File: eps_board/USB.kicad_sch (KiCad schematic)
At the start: 3 parts, among them J12 10155435-00011LF

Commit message: combine interrupts per powerline and use i2c expanders to turn on and solicit feedback
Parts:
- renumbered R122 to R98, R123 to R99
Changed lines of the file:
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@@
 		(dnp no)
 		(fields_autoplaced yes)
-		(property "Reference" "#PWR029"
+		(property "Reference" "#PWR033"
 			(at 114.3 89.535 0)
 			(effects
@@
 			(project "EPS"
 				(path "/05170af6-30ef-4c3a-b972-f098085da1bc/dffa178b-07a8-4735-b10c-32a6042c7f6e"
-					(reference "#PWR029")
+					(reference "#PWR033")
 					(unit 1)
 				)
@@
 		(on_board yes)
 		(dnp no)
-		(property "Reference" "R123"
+		(property "Reference" "R99"
 			(at 166.37 95.885 90)
 			(effects
@@
 			(project "EPS"
 				(path "/05170af6-30ef-4c3a-b972-f098085da1bc/dffa178b-07a8-4735-b10c-32a6042c7f6e"
-					(reference "R123")
+					(reference "R99")
 					(unit 1)
 				)
@@
 		(on_board yes)
 		(dnp no)
-		(property "Reference" "R122"
+		(property "Reference" "R98"
 			(at 120.65 80.645 90)
 			(effects
@@
 			(project "EPS"
 				(path "/05170af6-30ef-4c3a-b972-f098085da1bc/dffa178b-07a8-4735-b10c-32a6042c7f6e"
-					(reference "R122")
+					(reference "R98")
 					(unit 1)
 				)
@@
 		(dnp no)
 		(fields_autoplaced yes)
-		(property "Reference" "#PWR030"
+		(property "Reference" "#PWR034"
 			(at 172.72 99.695 0)
 			(effects
@@
 			(project "EPS"
 				(path "/05170af6-30ef-4c3a-b972-f098085da1bc/dffa178b-07a8-4735-b10c-32a6042c7f6e"
-					(reference "#PWR030")
+					(reference "#PWR034")
 					(unit 1)
 				)
@@
 		(dnp no)
 		(fields_autoplaced yes)
-		(property "Reference" "#PWR031"
+		(property "Reference" "#PWR035"
 			(at 161.29 117.475 0)
 			(effects
@@
 			(project "EPS"
 				(path "/05170af6-30ef-4c3a-b972-f098085da1bc/dffa178b-07a8-4735-b10c-32a6042c7f6e"
-					(reference "#PWR031")
+					(reference "#PWR035")
 					(unit 1)
 				)

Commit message: laying all the tracks, interim commit
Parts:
- added D1: ESD9B5.0ST5G, Diode_SMD:D_SOD-923, symbol Diode:ESD9B5.0ST5G
- added R167: 1M, Resistor_SMD:R_0402_1005Metric_Pad0.72x0.64mm_HandSolder, symbol Device:R
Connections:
- net GND: now also D1.2 (A2), R167.2
- net VBUS: now also D1.1 (A1), R167.1

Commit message: interim commit
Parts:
- added R1: 47K, Resistor_SMD:R_0402_1005Metric_Pad0.72x0.64mm_HandSolder, symbol Device:R
- R167: value 1M -> 91K
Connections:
- net VBUS: now also R1.1; no longer R167.1
- new net VBUS_GOOD: R1.2, R167.1
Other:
- moved on the sheet: R167
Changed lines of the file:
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@@
 	(paper "A4")
-	(junction
-		(at 189.865 83.185)
-		(diameter 0)
-		(color 0 0 0 0)
-	)
 	(junction
 		(at 177.165 78.105)
@@
 		(color 0 0 0 0)
 	)
-	(junction
-		(at 186.69 78.105)
-		(diameter 0)
-		(color 0 0 0 0)
-	)
 	(no_connect
 		(at 161.29 106.045)
@@
 	(wire
 		(pts
-			(xy 189.865 83.82) (xy 189.865 83.185)
-		)
-		(stroke
-			(width 0)
-			(type default)
-		)
-	)
-	(wire
-		(pts
-			(xy 189.865 83.185) (xy 191.135 83.185)
-		)
-		(stroke
-			(width 0)
-			(type default)
-		)
-	)
-	(wire
-		(pts
-			(xy 177.165 78.105) (xy 186.69 78.105)
+			(xy 177.165 78.105) (xy 191.135 78.105)
 		)
 		(stroke
@@
 	(wire
 		(pts
-			(xy 189.865 92.075) (xy 189.865 91.44)
-		)
-		(stroke
-			(width 0)
-			(type default)
-		)
-	)
-	(wire
-		(pts
-			(xy 186.69 83.185) (xy 189.865 83.185)
+			(xy 191.135 100.965) (xy 191.135 99.695)
 		)
 		(stroke
@@
 	(wire
 		(pts
+			(xy 191.135 88.265) (xy 191.135 92.075)
+		)
+		(stroke
+			(width 0)
+			(type default)
+		)
+	)
+	(wire
+		(pts
 			(xy 177.165 86.36) (xy 177.165 85.725)
 		)
@@
 	(wire
 		(pts
-			(xy 186.69 78.105) (xy 186.69 83.185)
-		)
-		(stroke
-			(width 0)
-			(type default)
-		)
-	)
-	(wire
-		(pts
-			(xy 186.69 78.105) (xy 191.135 78.105)
+			(xy 191.135 78.105) (xy 191.135 80.645)
 		)
 		(stroke
@@
 		)
 	)
+	(hierarchical_label "VBUS_GOOD"
+		(shape input)
+		(at 191.135 90.17 0)
+		(fields_autoplaced yes)
+		(effects
+			(font
+				(size 1.27 1.27)
+			)
+			(justify left)
+		)
+	)
 	(hierarchical_label "VBUS"
 		(shape input)
@@
 		)
 	)
-	(hierarchical_label "VBUS_GOOD"
+	(hierarchical_label "GND"
 		(shape input)
-		(at 191.135 83.185 0)
+		(at 191.135 100.965 180)
 		(fields_autoplaced yes)
 		(effects
@@
 				(size 1.27 1.27)
 			)
-			(justify left)
-		)
-	)
-	(hierarchical_label "GND"
+			(justify right)
+		)
+	)
+	(hierarchical_label "DN"
 		(shape input)
-		(at 189.865 92.075 180)
+		(at 181.61 88.265 0)
 		(fields_autoplaced yes)
 		(effects
@@
 				(size 1.27 1.27)
 			)
-			(justify right)
-		)
-	)
-	(hierarchical_label "DN"
-		(shape input)
-		(at 181.61 88.265 0)
-		(fields_autoplaced yes)
-		(effects
-			(font
-				(size 1.27 1.27)
-			)
 			(justify left)
+		)
+	)
+	(symbol
+		(lib_id "Device:R")
+		(at 191.135 84.455 0)
+		(unit 1)
+		(exclude_from_sim no)
+		(in_bom yes)
+		(on_board yes)
+		(dnp no)
+		(fields_autoplaced yes)
+		(property "Reference" "R1"
+			(at 193.04 83.1849 0)
+			(effects
+				(font
+					(size 1.27 1.27)
+				)
+				(justify left)
+			)
+		)
+		(property "Value" "47K"
+			(at 193.04 85.7249 0)
+			(effects
+				(font
+					(size 1.27 1.27)
+				)
+				(justify left)
+			)
+		)
+		(property "Footprint" "Resistor_SMD:R_0402_1005Metric_Pad0.72x0.64mm_HandSolder"
+			(at 189.357 84.455 90)
+			(effects
+				(font
+					(size 1.27 1.27)
+				)
+				(hide yes)
+			)
+		)
+		(property "Datasheet" "~"
+			(at 191.135 84.455 0)
+			(effects
+				(font
+					(size 1.27 1.27)
+				)
+				(hide yes)
+			)
+		)
+		(property "Description" "Resistor"
+			(at 191.135 84.455 0)
+			(effects
+				(font
+					(size 1.27 1.27)
+				)
+				(hide yes)
+			)
+		)
+		(pin "1"
+		)
+		(pin "2"
+		)
+		(instances
+			(project "EPS"
+				(path "/05170af6-30ef-4c3a-b972-f098085da1bc/dffa178b-07a8-4735-b10c-32a6042c7f6e"
+					(reference "R1")
+					(unit 1)
+				)
+			)
 		)
 	)
@@
 	(symbol
 		(lib_id "Device:R")
-		(at 189.865 87.63 0)
+		(at 191.135 95.885 0)
 		(unit 1)
 		(exclude_from_sim no)
@@
 		(fields_autoplaced yes)
 		(property "Reference" "R167"
-			(at 191.77 86.3599 0)
+			(at 193.04 94.6149 0)
 			(effects
 				(font
@@
 			)
 		)
-		(property "Value" "1M"
-			(at 191.77 88.8999 0)
+		(property "Value" "91K"
+			(at 193.04 97.1549 0)
 			(effects
 				(font
@@
 		)
 		(property "Footprint" "Resistor_SMD:R_0402_1005Metric_Pad0.72x0.64mm_HandSolder"
-			(at 188.087 87.63 90)
+			(at 189.357 95.885 90)
 			(effects
 				(font
@@
 		)
 		(property "Datasheet" "~"
-			(at 189.865 87.63 0)
+			(at 191.135 95.885 0)
 			(effects
 				(font
@@
 		)
 		(property "Description" "Resistor"
-			(at 189.865 87.63 0)
-			(effects
-				(font
+			(at 191.135 95.885 0)
+			(effects
+				(font

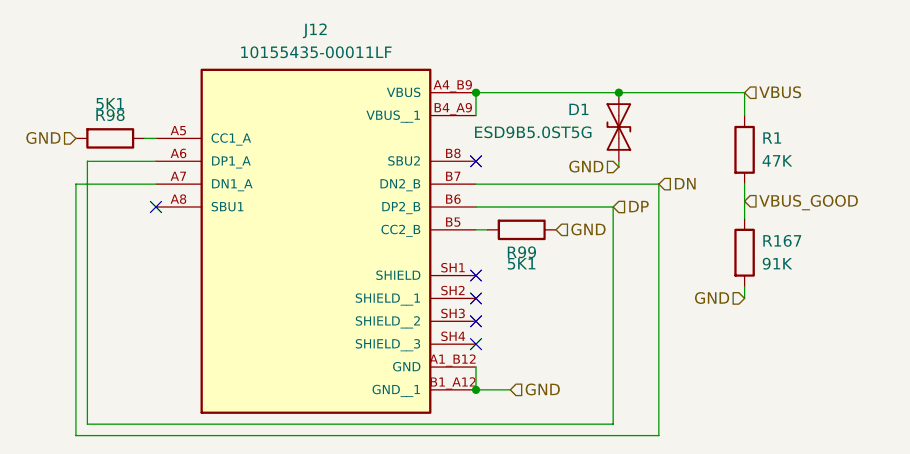
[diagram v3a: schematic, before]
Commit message: add 2V8 regulator and switch for SCI cameras, refactor switch/monitors with nonstandard voltage that require level shifting
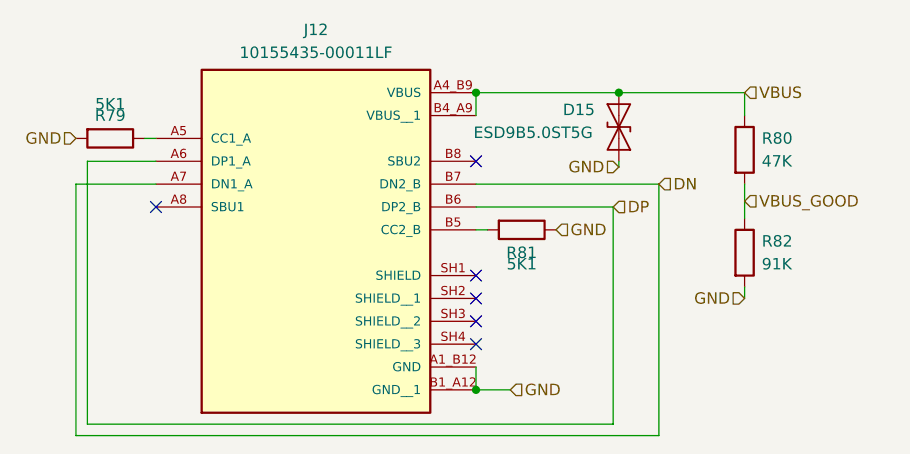
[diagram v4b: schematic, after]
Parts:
- renumbered D1 to D15, R98 to R79, R1 to R80, R99 to R81, R167 to R82
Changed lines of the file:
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@@
 		(dnp no)
 		(fields_autoplaced yes)
-		(property "Reference" "R1"
+		(property "Reference" "R80"
 			(at 193.04 83.1849 0)
 			(effects
@@
 			(project "EPS"
 				(path "/05170af6-30ef-4c3a-b972-f098085da1bc/dffa178b-07a8-4735-b10c-32a6042c7f6e"
-					(reference "R1")
+					(reference "R80")
 					(unit 1)
 				)
@@
 		(on_board yes)
 		(dnp no)
-		(property "Reference" "R99"
+		(property "Reference" "R81"
 			(at 166.37 95.885 90)
 			(effects
@@
 			(project "EPS"
 				(path "/05170af6-30ef-4c3a-b972-f098085da1bc/dffa178b-07a8-4735-b10c-32a6042c7f6e"
-					(reference "R99")
+					(reference "R81")
 					(unit 1)
 				)
@@
 		(on_board yes)
 		(dnp no)
-		(property "Reference" "R98"
+		(property "Reference" "R79"
 			(at 120.65 80.645 90)
 			(effects
@@
 			(project "EPS"
 				(path "/05170af6-30ef-4c3a-b972-f098085da1bc/dffa178b-07a8-4735-b10c-32a6042c7f6e"
-					(reference "R98")
+					(reference "R79")
 					(unit 1)
 				)
@@
 		(dnp no)
 		(fields_autoplaced yes)
-		(property "Reference" "R167"
+		(property "Reference" "R82"
 			(at 193.04 94.6149 0)
 			(effects
@@
 			(project ""
 				(path "/05170af6-30ef-4c3a-b972-f098085da1bc/dffa178b-07a8-4735-b10c-32a6042c7f6e"
-					(reference "R167")
+					(reference "R82")
 					(unit 1)
 				)
@@
 		(on_board yes)
 		(dnp no)
-		(property "Reference" "D1"
+		(property "Reference" "D15"
 			(at 172.72 80.01 90)
 			(effects
@@
 			(project "EPS"
 				(path "/05170af6-30ef-4c3a-b972-f098085da1bc/dffa178b-07a8-4735-b10c-32a6042c7f6e"
-					(reference "D1")
+					(reference "D15")
 					(unit 1)
 				)

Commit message: RSQ chip replaced with dual nor gates chips
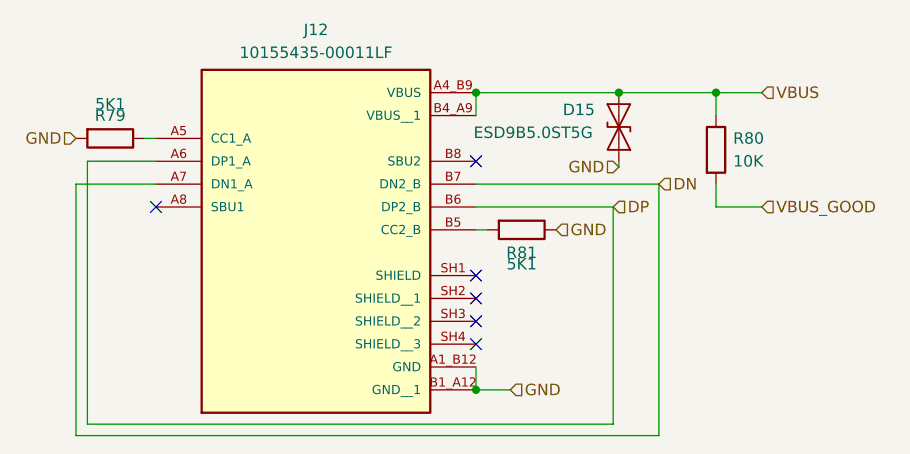
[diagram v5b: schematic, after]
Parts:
- removed R82: 91K, Resistor_SMD:R_0402_1005Metric_Pad0.72x0.64mm_HandSolder, symbol Device:R
- R80: value 47K -> 10K
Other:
- moved on the sheet: R80
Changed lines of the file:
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@@
+		(color 0 0 0 0)
+	)
+	(junction
+		(at 187.96 78.105)
+		(diameter 0)
 		(color 0 0 0 0)
 	)
@@
 	(wire
 		(pts
-			(xy 177.165 78.105) (xy 191.135 78.105)
+			(xy 193.04 78.105) (xy 187.96 78.105)
 		)
 		(stroke
@@
 	(wire
 		(pts
+			(xy 193.04 90.805) (xy 187.96 90.805)
+		)
+		(stroke
+			(width 0)
+			(type default)
+		)
+	)
+	(wire
+		(pts
+			(xy 177.165 78.105) (xy 187.96 78.105)
+		)
+		(stroke
+			(width 0)
+			(type default)
+		)
+	)
+	(wire
+		(pts
 			(xy 161.29 90.805) (xy 176.53 90.805)
 		)
@@
 	(wire
 		(pts
-			(xy 191.135 100.965) (xy 191.135 99.695)
-		)
-		(stroke
-			(width 0)
-			(type default)
-		)
-	)
-	(wire
-		(pts
 			(xy 116.84 116.205) (xy 116.84 88.265)
 		)
@@
 	(wire
 		(pts
-			(xy 191.135 88.265) (xy 191.135 92.075)
-		)
-		(stroke
-			(width 0)
-			(type default)
-		)
-	)
-	(wire
-		(pts
 			(xy 177.165 86.36) (xy 177.165 85.725)
 		)
@@
 	(wire
 		(pts
+			(xy 187.96 90.805) (xy 187.96 88.265)
+		)
+		(stroke
+			(width 0)
+			(type default)
+		)
+	)
+	(wire
+		(pts
 			(xy 116.84 88.265) (xy 125.73 88.265)
 		)
@@
 	(wire
 		(pts
-			(xy 191.135 78.105) (xy 191.135 80.645)
+			(xy 187.96 78.105) (xy 187.96 80.645)
 		)
 		(stroke
@@
 	(hierarchical_label "VBUS_GOOD"
 		(shape input)
-		(at 191.135 90.17 0)
+		(at 193.04 90.805 0)
 		(fields_autoplaced yes)
 		(effects
@@
 	(hierarchical_label "VBUS"
 		(shape input)
-		(at 191.135 78.105 0)
+		(at 193.04 78.105 0)
 		(fields_autoplaced yes)
 		(effects
@@
 		)
 	)
-	(hierarchical_label "GND"
+	(hierarchical_label "DN"
 		(shape input)
-		(at 191.135 100.965 180)
+		(at 181.61 88.265 0)
 		(fields_autoplaced yes)
 		(effects
@@
 				(size 1.27 1.27)
 			)
-			(justify right)
-		)
-	)
-	(hierarchical_label "DN"
-		(shape input)
-		(at 181.61 88.265 0)
-		(fields_autoplaced yes)
-		(effects
-			(font
-				(size 1.27 1.27)
-			)
 			(justify left)
 		)
@@
 	(symbol
 		(lib_id "Device:R")
-		(at 191.135 84.455 0)
+		(at 187.96 84.455 0)
 		(unit 1)
 		(exclude_from_sim no)
@@
 		(fields_autoplaced yes)
 		(property "Reference" "R80"
-			(at 193.04 83.1849 0)
+			(at 189.865 83.1849 0)
 			(effects
 				(font
@@
 			)
 		)
-		(property "Value" "47K"
-			(at 193.04 85.7249 0)
+		(property "Value" "10K"
+			(at 189.865 85.7249 0)
 			(effects
 				(font
@@
 		)
 		(property "Footprint" "Resistor_SMD:R_0402_1005Metric_Pad0.72x0.64mm_HandSolder"
-			(at 189.357 84.455 90)
+			(at 186.182 84.455 90)
 			(effects
 				(font
@@
 		)
 		(property "Datasheet" "~"
-			(at 191.135 84.455 0)
+			(at 187.96 84.455 0)
 			(effects
 				(font
@@
 		)
 		(property "Description" "Resistor"
-			(at 191.135 84.455 0)
+			(at 187.96 84.455 0)
 			(effects
 				(font
@@
 					(unit 1)
 				)
-			)
-		)
-	)
-	(symbol
-		(lib_id "Device:R")
-		(at 191.135 95.885 0)
-		(unit 1)
-		(exclude_from_sim no)
-		(in_bom yes)
-		(on_board yes)
-		(dnp no)
-		(fields_autoplaced yes)
-		(property "Reference" "R82"
-			(at 193.04 94.6149 0)
-			(effects
-				(font
-					(size 1.27 1.27)
-				)
-				(justify left)
-			)
-		)
-		(property "Value" "91K"
-			(at 193.04 97.1549 0)
-			(effects
-				(font
-					(size 1.27 1.27)
-				)
-				(justify left)
-			)
-		)
-		(property "Footprint" "Resistor_SMD:R_0402_1005Metric_Pad0.72x0.64mm_HandSolder"
-			(at 189.357 95.885 90)
-			(effects
-				(font
-					(size 1.27 1.27)
-				)
-				(hide yes)
-			)
-		)
-		(property "Datasheet" "~"
-			(at 191.135 95.885 0)
-			(effects
-				(font
-					(size 1.27 1.27)
-				)
-				(hide yes)
-			)
-		)
-		(property "Description" "Resistor"
-			(at 191.135 95.885 0)
-			(effects
-				(font
-					(size 1.27 1.27)
-				)
-				(hide yes)
-			)
-		)
-		(pin "1"
-		)
-		(pin "2"
-		)
-		(instances
-			(project ""
-				(path "/05170af6-30ef-4c3a-b972-f098085da1bc/dffa178b-07a8-4735-b10c-32a6042c7f6e"
-					(reference "R82")
-					(unit 1)
-				)

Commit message: connect all parallel solar panels to mcu
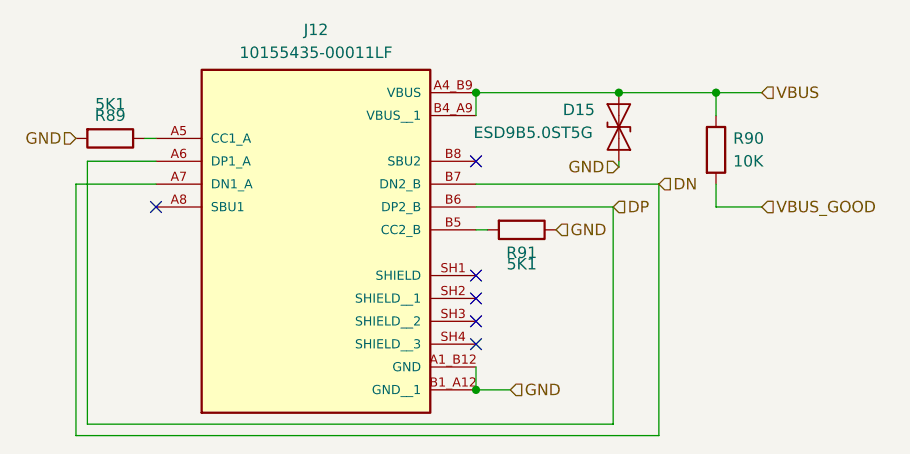
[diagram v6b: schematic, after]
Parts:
- renumbered R79 to R89, R80 to R90, R81 to R91
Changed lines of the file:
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@@
 		(dnp no)
 		(fields_autoplaced yes)
-		(property "Reference" "R80"
+		(property "Reference" "R90"
 			(at 189.865 83.1849 0)
 			(effects
@@
 			(project "EPS"
 				(path "/05170af6-30ef-4c3a-b972-f098085da1bc/dffa178b-07a8-4735-b10c-32a6042c7f6e"
-					(reference "R80")
+					(reference "R90")
 					(unit 1)
 				)
@@
 		(on_board yes)
 		(dnp no)
-		(property "Reference" "R81"
+		(property "Reference" "R91"
 			(at 166.37 95.885 90)
 			(effects
@@
 			(project "EPS"
 				(path "/05170af6-30ef-4c3a-b972-f098085da1bc/dffa178b-07a8-4735-b10c-32a6042c7f6e"
-					(reference "R81")
+					(reference "R91")
 					(unit 1)
 				)
@@
 		(on_board yes)
 		(dnp no)
-		(property "Reference" "R79"
+		(property "Reference" "R89"
 			(at 120.65 80.645 90)
 			(effects
@@
 			(project "EPS"
 				(path "/05170af6-30ef-4c3a-b972-f098085da1bc/dffa178b-07a8-4735-b10c-32a6042c7f6e"
-					(reference "R79")
+					(reference "R89")
 					(unit 1)
 				)

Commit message: flip CAN high low around to ease access from the front side
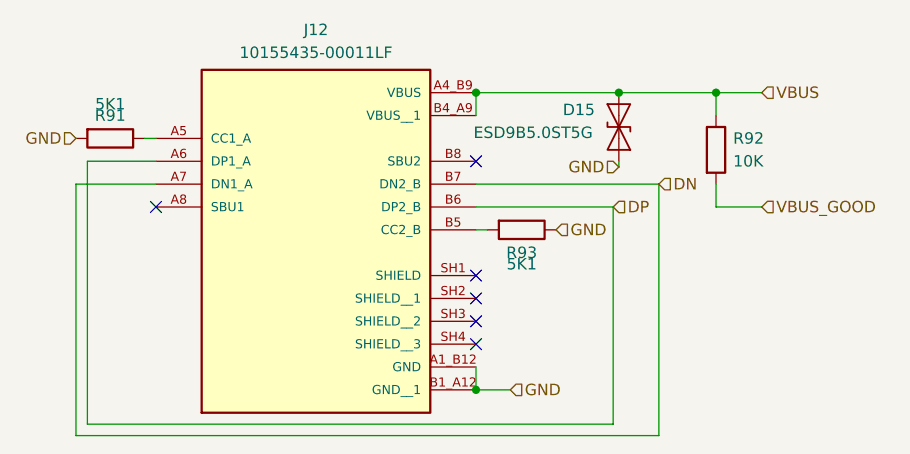
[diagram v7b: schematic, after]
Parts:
- renumbered R89 to R91, R90 to R92, R91 to R93
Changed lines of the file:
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@@
 		(dnp no)
 		(fields_autoplaced yes)
-		(property "Reference" "R90"
+		(property "Reference" "R92"
 			(at 189.865 83.1849 0)
 			(effects
@@
 			(project "EPS"
 				(path "/05170af6-30ef-4c3a-b972-f098085da1bc/dffa178b-07a8-4735-b10c-32a6042c7f6e"
-					(reference "R90")
+					(reference "R92")
 					(unit 1)
 				)
@@
 		(on_board yes)
 		(dnp no)
-		(property "Reference" "R91"
+		(property "Reference" "R93"
 			(at 166.37 95.885 90)
 			(effects
@@
 			(project "EPS"
 				(path "/05170af6-30ef-4c3a-b972-f098085da1bc/dffa178b-07a8-4735-b10c-32a6042c7f6e"
-					(reference "R91")
+					(reference "R93")
 					(unit 1)
 				)
@@
 		(on_board yes)
 		(dnp no)
-		(property "Reference" "R89"
+		(property "Reference" "R91"
 			(at 120.65 80.645 90)
 			(effects
@@
 			(project "EPS"
 				(path "/05170af6-30ef-4c3a-b972-f098085da1bc/dffa178b-07a8-4735-b10c-32a6042c7f6e"
-					(reference "R89")
+					(reference "R91")
 					(unit 1)
 				)

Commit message: replace nearly all buck converters with boost buck (missing is 5raw
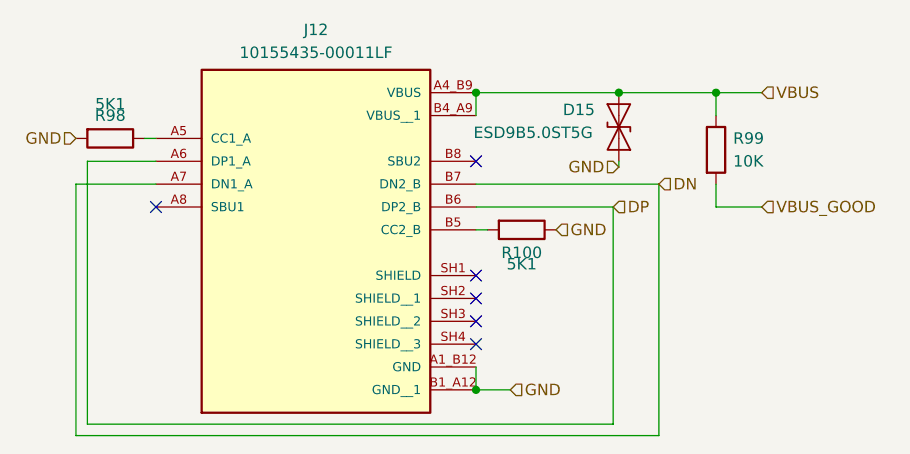
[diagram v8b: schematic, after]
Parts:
- renumbered R93 to R100, R91 to R98, R92 to R99
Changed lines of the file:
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@@
 		(dnp no)
 		(fields_autoplaced yes)
-		(property "Reference" "R92"
+		(property "Reference" "R99"
 			(at 189.865 83.1849 0)
 			(effects
@@
 			(project "EPS"
 				(path "/05170af6-30ef-4c3a-b972-f098085da1bc/dffa178b-07a8-4735-b10c-32a6042c7f6e"
-					(reference "R92")
+					(reference "R99")
 					(unit 1)
 				)
@@
 		(on_board yes)
 		(dnp no)
-		(property "Reference" "R93"
+		(property "Reference" "R100"
 			(at 166.37 95.885 90)
 			(effects
@@
 			(project "EPS"
 				(path "/05170af6-30ef-4c3a-b972-f098085da1bc/dffa178b-07a8-4735-b10c-32a6042c7f6e"
-					(reference "R93")
+					(reference "R100")
 					(unit 1)
 				)
@@
 		(on_board yes)
 		(dnp no)
-		(property "Reference" "R91"
+		(property "Reference" "R98"
 			(at 120.65 80.645 90)
 			(effects
@@
 			(project "EPS"
 				(path "/05170af6-30ef-4c3a-b972-f098085da1bc/dffa178b-07a8-4735-b10c-32a6042c7f6e"
-					(reference "R91")
+					(reference "R98")
 					(unit 1)
 				)
